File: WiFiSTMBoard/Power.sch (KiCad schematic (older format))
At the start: 6 parts

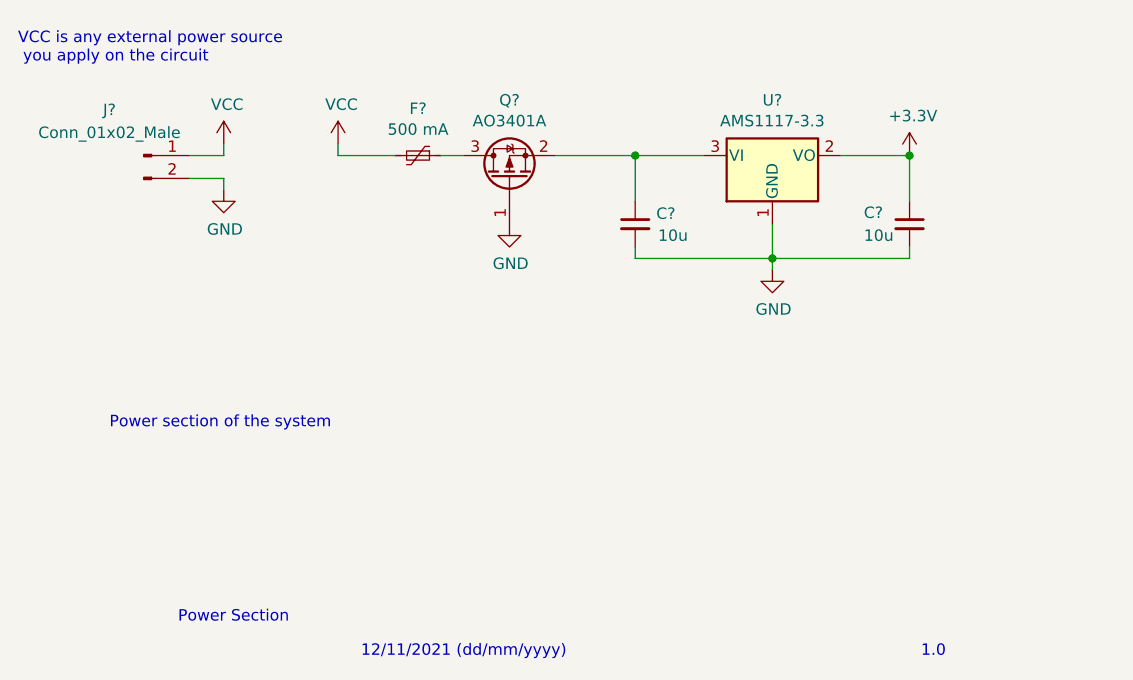
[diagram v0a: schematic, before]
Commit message: added esp8266
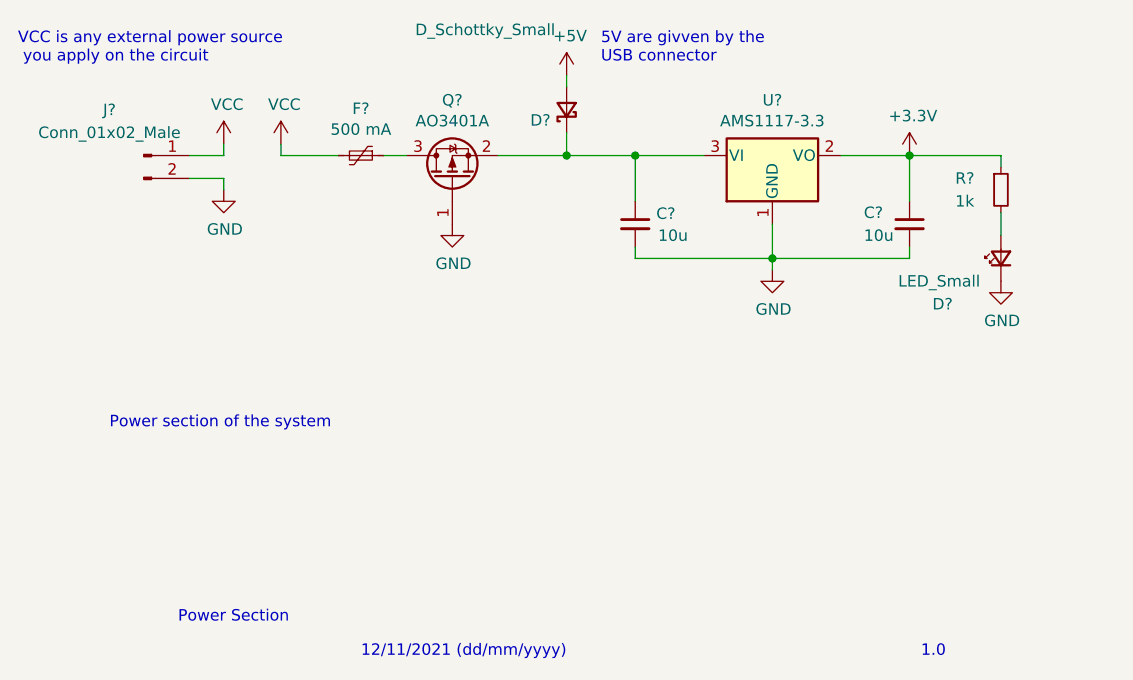
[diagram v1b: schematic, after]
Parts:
- added D?: D_Schottky_Small, symbol Device:D_Schottky_Small
- added D?: LED_Small, symbol Device:LED_Small
- added R?: 1k, symbol Device:R_Small
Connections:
- net +3V3: now also R?.1
- net GND: now also D?.1 (K)
- net at C?.1, Q?.2 (S), U?.3 (VI): now also D?.1 (K)
- new net: D?.2 (A), R?.2
- new net +5V: D?.2 (A)
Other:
- note added: "5V are givven by the\nUSB connector"
- moved on the sheet: F?, Q?
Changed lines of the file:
@@
 $Descr User 5906 4016
 encoding utf-8
-Sheet 2 5
+Sheet 2 6
 Title ""
 Date ""
@@
 L Device:Polyfuse_Small F?
 U 1 1 619B5F71
-P 2600 1200
-F 0 "F?" V 2395 1200 50  0000 C CNN
-F 1 "500 mA" V 2486 1200 50  0000 C CNN
-F 2 "" H 2650 1000 50  0001 L CNN
-F 3 "~" H 2600 1200 50  0001 C CNN
-	1    2600 1200
+P 2350 1200
+F 0 "F?" V 2145 1200 50  0000 C CNN
+F 1 "500 mA" V 2236 1200 50  0000 C CNN
+F 2 "" H 2400 1000 50  0001 L CNN
+F 3 "~" H 2350 1200 50  0001 C CNN
+	1    2350 1200
 	0    1    1    0
 $EndComp
 Wire Wire Line
-	2250 1150 2250 1200
-Wire Wire Line
-	2500 1200 2250 1200
+	2000 1150 2000 1200
+Wire Wire Line
+	2250 1200 2000 1200
 $Comp
 L Transistor_FET:AO3401A Q?
 U 1 1 619B8247
-P 3000 1300
-F 0 "Q?" V 3342 1300 50  0000 C CNN
-F 1 "AO3401A" V 3251 1300 50  0000 C CNN
-F 2 "Package_TO_SOT_SMD:SOT-23" H 3200 1225 50  0001 L CIN
-F 3 "http://www.aosmd.com/pdfs/datasheet/AO3401A.pdf" H 3000 1300 50  0001 L CNN
-	1    3000 1300
+P 2750 1300
+F 0 "Q?" V 3092 1300 50  0000 C CNN
+F 1 "AO3401A" V 3001 1300 50  0000 C CNN
+F 2 "Package_TO_SOT_SMD:SOT-23" H 2950 1225 50  0001 L CIN
+F 3 "http://www.aosmd.com/pdfs/datasheet/AO3401A.pdf" H 2750 1300 50  0001 L CNN
+	1    2750 1300
 	0    -1   -1   0
 $EndComp
 Wire Wire Line
-	2700 1200 2800 1200
+	2450 1200 2550 1200
 $Comp
 L power:GND #PWR?
 U 1 1 619BB1C5
-P 3000 1500
-F 0 "#PWR?" H 3000 1250 50  0001 C CNN
-F 1 "GND" H 3005 1327 50  0000 C CNN
-F 2 "" H 3000 1500 50  0001 C CNN
-F 3 "" H 3000 1500 50  0001 C CNN
-	1    3000 1500
-	1    0    0    -1
-$EndComp
-Wire Wire Line
-	3200 1200 3550 1200
-Connection ~ 3550 1200
+P 2750 1500
+F 0 "#PWR?" H 2750 1250 50  0001 C CNN
+F 1 "GND" H 2755 1327 50  0000 C CNN
+F 2 "" H 2750 1500 50  0001 C CNN
+F 3 "" H 2750 1500 50  0001 C CNN
+	1    2750 1500
+	1    0    0    -1
+$EndComp
 $Comp
 L power:+3.3V #PWR?
@@
 L power:VCC #PWR?
 U 1 1 619C9B76
-P 2250 1150
-F 0 "#PWR?" H 2250 1000 50  0001 C CNN
-F 1 "VCC" H 2265 1323 50  0000 C CNN
-F 2 "" H 2250 1150 50  0001 C CNN
-F 3 "" H 2250 1150 50  0001 C CNN
-	1    2250 1150
+P 2000 1150
+F 0 "#PWR?" H 2000 1000 50  0001 C CNN
+F 1 "VCC" H 2015 1323 50  0000 C CNN
+F 2 "" H 2000 1150 50  0001 C CNN
+F 3 "" H 2000 1150 50  0001 C CNN
+	1    2000 1150
 	1    0    0    -1
 $EndComp
 Text Notes 850  800  0    50   ~ 0
 VCC is any external power source\n you apply on the circuit
+Wire Wire Line
+	2950 1200 3250 1200
+Connection ~ 3550 1200
+$Comp
+L Device:D_Schottky_Small D?
+U 1 1 6195F1EF
+P 3250 1000
+F 0 "D?" V 3204 1070 50  0000 L CNN
+F 1 "D_Schottky_Small" V 3600 1050 50  0000 L CNN
+F 2 "" V 3250 1000 50  0001 C CNN
+F 3 "~" V 3250 1000 50  0001 C CNN
+	1    3250 1000
+	0    -1   -1   0
+$EndComp
+Wire Wire Line
+	3250 1100 3250 1200
+Connection ~ 3250 1200
+Wire Wire Line
+	3250 1200 3550 1200
+$Comp
+L power:+5V #PWR?
+U 1 1 61960D48
+P 3250 850
+F 0 "#PWR?" H 3250 700 50  0001 C CNN
+F 1 "+5V" H 3265 1023 50  0000 C CNN
+F 2 "" H 3250 850 50  0001 C CNN
+F 3 "" H 3250 850 50  0001 C CNN
+	1    3250 850
+	1    0    0    -1
+$EndComp
+Wire Wire Line
+	3250 850  3250 900
+Text Notes 3400 800  0    50   ~ 0
+5V are givven by the\nUSB connector
+$Comp
+L Device:R_Small R?
+U 1 1 61976B04
+P 5150 1350
+F 0 "R?" H 4950 1400 50  0000 L CNN
+F 1 "1k" H 4950 1300 50  0000 L CNN
+F 2 "" H 5150 1350 50  0001 C CNN
+F 3 "~" H 5150 1350 50  0001 C CNN
+	1    5150 1350
+	1    0    0    -1
+$EndComp
+$Comp
+L Device:LED_Small D?
+U 1 1 61977926
+P 5150 1650
+F 0 "D?" V 4950 1950 50  0000 R CNN
+F 1 "LED_Small" V 5050 2100 50  0000 R CNN
+F 2 "" V 5150 1650 50  0001 C CNN
+F 3 "~" V 5150 1650 50  0001 C CNN
+	1    5150 1650
+	0    -1   -1   0
+$EndComp
+Wire Wire Line
+	5150 1450 5150 1550
+$Comp
+L power:GND #PWR?
+U 1 1 61978BF6
+P 5150 1750
+F 0 "#PWR?" H 5150 1500 50  0001 C CNN
+F 1 "GND" H 5155 1577 50  0000 C CNN
+F 2 "" H 5150 1750 50  0001 C CNN
+F 3 "" H 5150 1750 50  0001 C CNN
+	1    5150 1750
+	1    0    0    -1
+$EndComp
+Wire Wire Line
+	4750 1200 5150 1200
+Wire Wire Line
+	5150 1200 5150 1250
 $EndSCHEMATC

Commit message: finished serial circuit
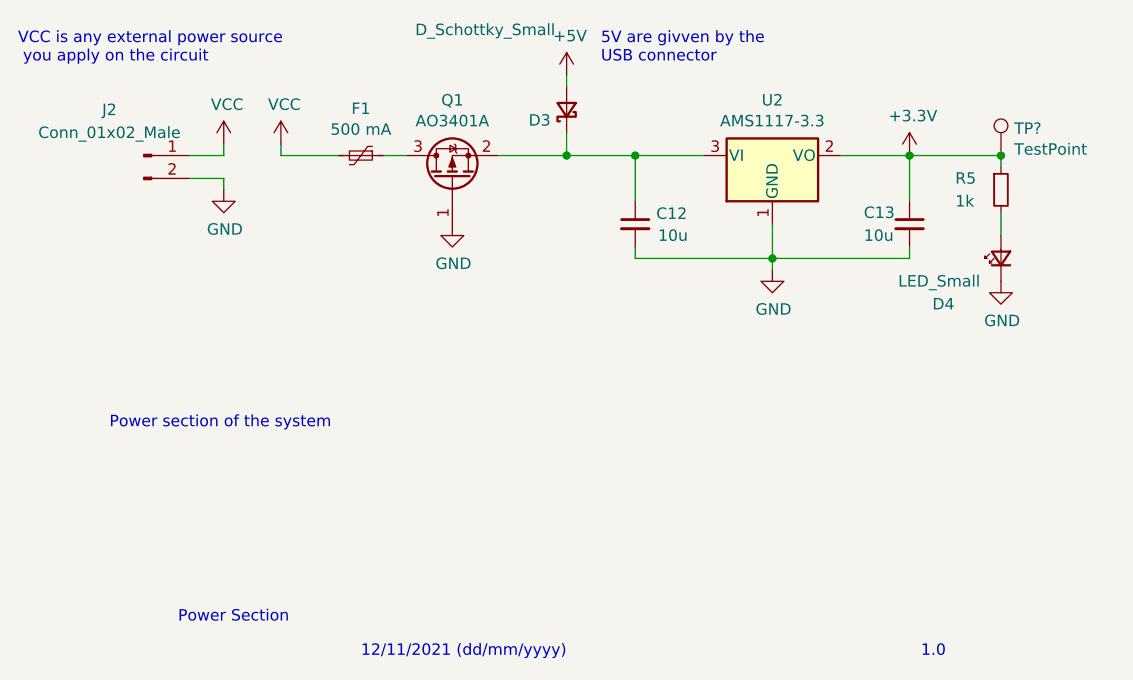
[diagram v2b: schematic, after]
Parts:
- added TP?: TestPoint, symbol Connector:TestPoint
- gave numbers to parts that had none: 9
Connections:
- net +3V3: now also TP?.1
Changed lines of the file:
@@
 12/11/2021 (dd/mm/yyyy)
 $Comp
-L Regulator_Linear:AMS1117-3.3 U?
+L Regulator_Linear:AMS1117-3.3 U2
 U 1 1 619A97DE
 P 4150 1200
-F 0 "U?" H 4150 1442 50  0000 C CNN
+F 0 "U2" H 4150 1442 50  0000 C CNN
 F 1 "AMS1117-3.3" H 4150 1351 50  0000 C CNN
 F 2 "Package_TO_SOT_SMD:SOT-223-3_TabPin2" H 4150 1400 50  0001 C CNN
@@
 $EndComp
 $Comp
-L power:GND #PWR?
+L power:GND #PWR0116
 U 1 1 619ABDEC
 P 4150 1700
-F 0 "#PWR?" H 4150 1450 50  0001 C CNN
+F 0 "#PWR0116" H 4150 1450 50  0001 C CNN
 F 1 "GND" H 4155 1527 50  0000 C CNN
 F 2 "" H 4150 1700 50  0001 C CNN
@@
 	4750 1650 4150 1650
 $Comp
-L Device:C_Small C?
+L Device:C_Small C13
 U 1 1 619AC998
 P 4750 1500
-F 0 "C?" H 4550 1550 50  0000 L CNN
+F 0 "C13" H 4550 1550 50  0000 L CNN
 F 1 "10u" H 4550 1450 50  0000 L CNN
 F 2 "" H 4750 1500 50  0001 C CNN
@@
 $EndComp
 $Comp
-L Device:C_Small C?
+L Device:C_Small C12
 U 1 1 619AC197
 P 3550 1500
-F 0 "C?" H 3642 1546 50  0000 L CNN
+F 0 "C12" H 3642 1546 50  0000 L CNN
 F 1 "10u" H 3650 1450 50  0000 L CNN
 F 2 "" H 3550 1500 50  0001 C CNN
@@
 $EndComp
 $Comp
-L Connector:Conn_01x02_Male J?
+L Connector:Conn_01x02_Male J2
 U 1 1 619B17DC
 P 1400 1200
-F 0 "J?" H 1250 1400 50  0000 C CNN
+F 0 "J2" H 1250 1400 50  0000 C CNN
 F 1 "Conn_01x02_Male" H 1250 1300 50  0000 C CNN
 F 2 "" H 1400 1200 50  0001 C CNN
@@
 $EndComp
 $Comp
-L power:GND #PWR?
+L power:GND #PWR0117
 U 1 1 619B2697
 P 1750 1350
-F 0 "#PWR?" H 1750 1100 50  0001 C CNN
+F 0 "#PWR0117" H 1750 1100 50  0001 C CNN
 F 1 "GND" H 1755 1177 50  0000 C CNN
 F 2 "" H 1750 1350 50  0001 C CNN
@@
 	1750 1300 1750 1350
 $Comp
-L Device:Polyfuse_Small F?
+L Device:Polyfuse_Small F1
 U 1 1 619B5F71
 P 2350 1200
-F 0 "F?" V 2145 1200 50  0000 C CNN
+F 0 "F1" V 2145 1200 50  0000 C CNN
 F 1 "500 mA" V 2236 1200 50  0000 C CNN
 F 2 "" H 2400 1000 50  0001 L CNN
@@
 	2250 1200 2000 1200
 $Comp
-L Transistor_FET:AO3401A Q?
+L Transistor_FET:AO3401A Q1
 U 1 1 619B8247
 P 2750 1300
-F 0 "Q?" V 3092 1300 50  0000 C CNN
+F 0 "Q1" V 3092 1300 50  0000 C CNN
 F 1 "AO3401A" V 3001 1300 50  0000 C CNN
 F 2 "Package_TO_SOT_SMD:SOT-23" H 2950 1225 50  0001 L CIN
@@
 	2450 1200 2550 1200
 $Comp
-L power:GND #PWR?
+L power:GND #PWR0118
 U 1 1 619BB1C5
 P 2750 1500
-F 0 "#PWR?" H 2750 1250 50  0001 C CNN
+F 0 "#PWR0118" H 2750 1250 50  0001 C CNN
 F 1 "GND" H 2755 1327 50  0000 C CNN
 F 2 "" H 2750 1500 50  0001 C CNN
@@
 $EndComp
 $Comp
-L power:+3.3V #PWR?
+L power:+3.3V #PWR0119
 U 1 1 619BBADD
 P 4750 1200
-F 0 "#PWR?" H 4750 1050 50  0001 C CNN
+F 0 "#PWR0119" H 4750 1050 50  0001 C CNN
 F 1 "+3.3V" H 4765 1373 50  0000 C CNN
 F 2 "" H 4750 1200 50  0001 C CNN
@@
 Connection ~ 4750 1200
 $Comp
-L power:VCC #PWR?
+L power:VCC #PWR0120
 U 1 1 619C91C5
 P 1750 1150
-F 0 "#PWR?" H 1750 1000 50  0001 C CNN
+F 0 "#PWR0120" H 1750 1000 50  0001 C CNN
 F 1 "VCC" H 1765 1323 50  0000 C CNN
 F 2 "" H 1750 1150 50  0001 C CNN
@@
 $EndComp
 $Comp
-L power:VCC #PWR?
+L power:VCC #PWR0121
 U 1 1 619C9B76
 P 2000 1150
-F 0 "#PWR?" H 2000 1000 50  0001 C CNN
+F 0 "#PWR0121" H 2000 1000 50  0001 C CNN
 F 1 "VCC" H 2015 1323 50  0000 C CNN
 F 2 "" H 2000 1150 50  0001 C CNN
@@
 Connection ~ 3550 1200
 $Comp
-L Device:D_Schottky_Small D?
+L Device:D_Schottky_Small D3
 U 1 1 6195F1EF
 P 3250 1000
-F 0 "D?" V 3204 1070 50  0000 L CNN
+F 0 "D3" V 3204 1070 50  0000 L CNN
 F 1 "D_Schottky_Small" V 3600 1050 50  0000 L CNN
 F 2 "" V 3250 1000 50  0001 C CNN
@@
 	3250 1200 3550 1200
 $Comp
-L power:+5V #PWR?
+L power:+5V #PWR0122
 U 1 1 61960D48
 P 3250 850
-F 0 "#PWR?" H 3250 700 50  0001 C CNN
+F 0 "#PWR0122" H 3250 700 50  0001 C CNN
 F 1 "+5V" H 3265 1023 50  0000 C CNN
 F 2 "" H 3250 850 50  0001 C CNN
@@
 5V are givven by the\nUSB connector
 $Comp
-L Device:R_Small R?
+L Device:R_Small R5
 U 1 1 61976B04
 P 5150 1350
-F 0 "R?" H 4950 1400 50  0000 L CNN
+F 0 "R5" H 4950 1400 50  0000 L CNN
 F 1 "1k" H 4950 1300 50  0000 L CNN
 F 2 "" H 5150 1350 50  0001 C CNN
@@
 $EndComp
 $Comp
-L Device:LED_Small D?
+L Device:LED_Small D4
 U 1 1 61977926
 P 5150 1650
-F 0 "D?" V 4950 1950 50  0000 R CNN
+F 0 "D4" V 4950 1950 50  0000 R CNN
 F 1 "LED_Small" V 5050 2100 50  0000 R CNN
 F 2 "" V 5150 1650 50  0001 C CNN
@@
 	5150 1450 5150 1550
 $Comp
-L power:GND #PWR?
+L power:GND #PWR0123
 U 1 1 61978BF6
 P 5150 1750
-F 0 "#PWR?" H 5150 1500 50  0001 C CNN
+F 0 "#PWR0123" H 5150 1500 50  0001 C CNN
 F 1 "GND" H 5155 1577 50  0000 C CNN
 F 2 "" H 5150 1750 50  0001 C CNN
@@
 Wire Wire Line
 	5150 1200 5150 1250
+$Comp
+L Connector:TestPoint TP?
+U 1 1 61A42B7E
+P 5150 1200
+F 0 "TP?" H 5208 1318 50  0000 L CNN
+F 1 "TestPoint" H 5208 1227 50  0000 L CNN
+F 2 "" H 5350 1200 50  0001 C CNN
+F 3 "~" H 5350 1200 50  0001 C CNN
+	1    5150 1200
+	1    0    0    -1
+$EndComp
+Connection ~ 5150 1200
 $EndSCHEMATC

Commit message: starting PCB layout
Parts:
- added TP4, TP5: TP, TestPoint:TestPoint_Pad_D2.0mm, symbol Connector:TestPoint
- C12, C13: footprint (none) -> Capacitor_SMD:C_1206_3216Metric
- D3: footprint (none) -> Diode_SMD:D_SOD-123
- D4: footprint (none) -> LED_SMD:LED_1206_3216Metric
- F1: footprint (none) -> Fuse:Fuse_1206_3216Metric
- J2: footprint (none) -> Connector_Molex:Molex_KK-396_A-41791-0002_1x02_P3.96mm_Vertical
- R5: footprint (none) -> Resistor_SMD:R_1206_3216Metric
- TP6: renamed from TP?; value TestPoint -> TP; footprint (none) -> TestPoint:TestPoint_Pad_D2.0mm
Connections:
- net VCC: now also TP4.1
- net at C12.1, D3.1 (K), Q1.2 (S)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: now also TP5.1
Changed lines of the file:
@@
 $Descr User 5906 4016
 encoding utf-8
-Sheet 2 6
+Sheet 2 5
 Title ""
 Date ""
@@
 $EndComp
 $Comp
-L power:GND #PWR0116
+L power:GND #PWR022
 U 1 1 619ABDEC
 P 4150 1700
-F 0 "#PWR0116" H 4150 1450 50  0001 C CNN
+F 0 "#PWR022" H 4150 1450 50  0001 C CNN
 F 1 "GND" H 4155 1527 50  0000 C CNN
 F 2 "" H 4150 1700 50  0001 C CNN
@@
 F 0 "C13" H 4550 1550 50  0000 L CNN
 F 1 "10u" H 4550 1450 50  0000 L CNN
-F 2 "" H 4750 1500 50  0001 C CNN
+F 2 "Capacitor_SMD:C_1206_3216Metric" H 4750 1500 50  0001 C CNN
 F 3 "~" H 4750 1500 50  0001 C CNN
 	1    4750 1500
@@
 F 0 "C12" H 3642 1546 50  0000 L CNN
 F 1 "10u" H 3650 1450 50  0000 L CNN
-F 2 "" H 3550 1500 50  0001 C CNN
+F 2 "Capacitor_SMD:C_1206_3216Metric" H 3550 1500 50  0001 C CNN
 F 3 "~" H 3550 1500 50  0001 C CNN
 	1    3550 1500
@@
 F 0 "J2" H 1250 1400 50  0000 C CNN
 F 1 "Conn_01x02_Male" H 1250 1300 50  0000 C CNN
-F 2 "" H 1400 1200 50  0001 C CNN
+F 2 "Connector_Molex:Molex_KK-396_A-41791-0002_1x02_P3.96mm_Vertical" H 1400 1200 50  0001 C CNN
 F 3 "~" H 1400 1200 50  0001 C CNN
 	1    1400 1200
@@
 $EndComp
 $Comp
-L power:GND #PWR0117
+L power:GND #PWR020
 U 1 1 619B2697
 P 1750 1350
-F 0 "#PWR0117" H 1750 1100 50  0001 C CNN
+F 0 "#PWR020" H 1750 1100 50  0001 C CNN
 F 1 "GND" H 1755 1177 50  0000 C CNN
 F 2 "" H 1750 1350 50  0001 C CNN
@@
 F 0 "F1" V 2145 1200 50  0000 C CNN
 F 1 "500 mA" V 2236 1200 50  0000 C CNN
-F 2 "" H 2400 1000 50  0001 L CNN
+F 2 "Fuse:Fuse_1206_3216Metric" H 2400 1000 50  0001 L CNN
 F 3 "~" H 2350 1200 50  0001 C CNN
 	1    2350 1200
@@
 	2450 1200 2550 1200
 $Comp
-L power:GND #PWR0118
+L power:GND #PWR021
 U 1 1 619BB1C5
 P 2750 1500
-F 0 "#PWR0118" H 2750 1250 50  0001 C CNN
+F 0 "#PWR021" H 2750 1250 50  0001 C CNN
 F 1 "GND" H 2755 1327 50  0000 C CNN
 F 2 "" H 2750 1500 50  0001 C CNN
@@
 $EndComp
 $Comp
-L power:+3.3V #PWR0119
+L power:+3.3V #PWR019
 U 1 1 619BBADD
 P 4750 1200
-F 0 "#PWR0119" H 4750 1050 50  0001 C CNN
+F 0 "#PWR019" H 4750 1050 50  0001 C CNN
 F 1 "+3.3V" H 4765 1373 50  0000 C CNN
 F 2 "" H 4750 1200 50  0001 C CNN
@@
 Connection ~ 4750 1200
 $Comp
-L power:VCC #PWR0120
+L power:VCC #PWR017
 U 1 1 619C91C5
 P 1750 1150
-F 0 "#PWR0120" H 1750 1000 50  0001 C CNN
+F 0 "#PWR017" H 1750 1000 50  0001 C CNN
 F 1 "VCC" H 1765 1323 50  0000 C CNN
 F 2 "" H 1750 1150 50  0001 C CNN
@@
 $EndComp
 $Comp
-L power:VCC #PWR0121
+L power:VCC #PWR018
 U 1 1 619C9B76
 P 2000 1150
-F 0 "#PWR0121" H 2000 1000 50  0001 C CNN
+F 0 "#PWR018" H 2000 1000 50  0001 C CNN
 F 1 "VCC" H 2015 1323 50  0000 C CNN
 F 2 "" H 2000 1150 50  0001 C CNN
@@
 F 0 "D3" V 3204 1070 50  0000 L CNN
 F 1 "D_Schottky_Small" V 3600 1050 50  0000 L CNN
-F 2 "" V 3250 1000 50  0001 C CNN
+F 2 "Diode_SMD:D_SOD-123" V 3250 1000 50  0001 C CNN
 F 3 "~" V 3250 1000 50  0001 C CNN
 	1    3250 1000
@@
 	3250 1200 3550 1200
 $Comp
-L power:+5V #PWR0122
+L power:+5V #PWR016
 U 1 1 61960D48
 P 3250 850
-F 0 "#PWR0122" H 3250 700 50  0001 C CNN
+F 0 "#PWR016" H 3250 700 50  0001 C CNN
 F 1 "+5V" H 3265 1023 50  0000 C CNN
 F 2 "" H 3250 850 50  0001 C CNN
@@
 F 0 "R5" H 4950 1400 50  0000 L CNN
 F 1 "1k" H 4950 1300 50  0000 L CNN
-F 2 "" H 5150 1350 50  0001 C CNN
+F 2 "Resistor_SMD:R_1206_3216Metric" H 5150 1350 50  0001 C CNN
 F 3 "~" H 5150 1350 50  0001 C CNN
 	1    5150 1350
@@
 F 0 "D4" V 4950 1950 50  0000 R CNN
 F 1 "LED_Small" V 5050 2100 50  0000 R CNN
-F 2 "" V 5150 1650 50  0001 C CNN
+F 2 "LED_SMD:LED_1206_3216Metric" V 5150 1650 50  0001 C CNN
 F 3 "~" V 5150 1650 50  0001 C CNN
 	1    5150 1650
@@
 	5150 1450 5150 1550
 $Comp
-L power:GND #PWR0123
+L power:GND #PWR023
 U 1 1 61978BF6
 P 5150 1750
-F 0 "#PWR0123" H 5150 1500 50  0001 C CNN
+F 0 "#PWR023" H 5150 1500 50  0001 C CNN
 F 1 "GND" H 5155 1577 50  0000 C CNN
 F 2 "" H 5150 1750 50  0001 C CNN
@@
 	5150 1200 5150 1250
 $Comp
-L Connector:TestPoint TP?
+L Connector:TestPoint TP6
 U 1 1 61A42B7E
 P 5150 1200
-F 0 "TP?" H 5208 1318 50  0000 L CNN
-F 1 "TestPoint" H 5208 1227 50  0000 L CNN
-F 2 "" H 5350 1200 50  0001 C CNN
+F 0 "TP6" H 5208 1318 50  0000 L CNN
+F 1 "TP" H 5208 1227 50  0000 L CNN
+F 2 "TestPoint:TestPoint_Pad_D2.0mm" H 5350 1200 50  0001 C CNN
 F 3 "~" H 5350 1200 50  0001 C CNN
 	1    5150 1200
@@
 $EndComp
 Connection ~ 5150 1200
+$Comp
+L Connector:TestPoint TP5
+U 1 1 61A471E1
+P 3550 1200
+F 0 "TP5" H 3608 1318 50  0000 L CNN
+F 1 "TP" H 3608 1227 50  0000 L CNN
+F 2 "TestPoint:TestPoint_Pad_D2.0mm" H 3750 1200 50  0001 C CNN
+F 3 "~" H 3750 1200 50  0001 C CNN
+	1    3550 1200
+	1    0    0    -1
+$EndComp
+$Comp
+L Connector:TestPoint TP4
+U 1 1 61A47505
+P 2000 1200
+F 0 "TP4" H 1942 1226 50  0000 R CNN
+F 1 "TP" H 1942 1317 50  0000 R CNN
+F 2 "TestPoint:TestPoint_Pad_D2.0mm" H 2200 1200 50  0001 C CNN
+F 3 "~" H 2200 1200 50  0001 C CNN
+	1    2000 1200
+	-1   0    0    1
+$EndComp
+Connection ~ 2000 1200
 $EndSCHEMATC
